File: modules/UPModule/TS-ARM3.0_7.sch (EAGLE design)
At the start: 83 parts, among them IC1 LPC1115, IC100 BD9G101, P1 , P10 , P11 , P12 , P13 , P14 , P2 , P3 , P4 , P5 , P6 , P7 , P8 , P9 , T1 BC856, T2 BCP52, T3 BC847, X1 EIB

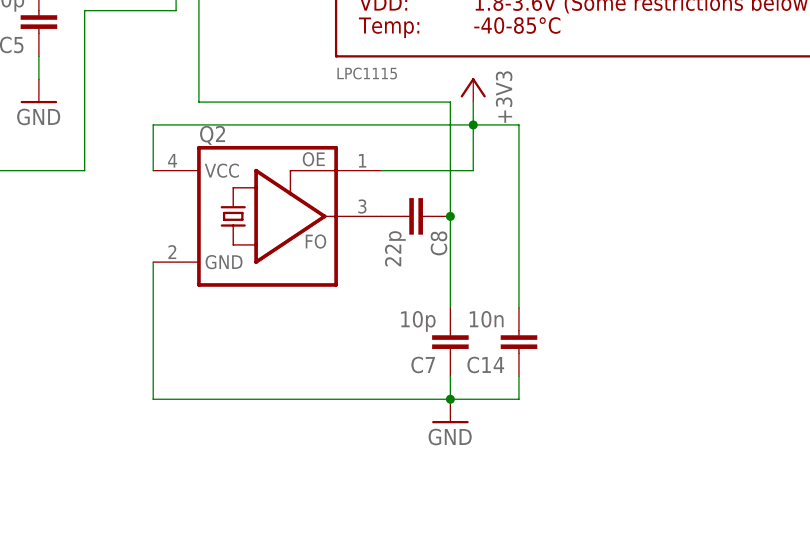
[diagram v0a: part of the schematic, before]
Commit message: value cap divider changed, micro vias with tstop, and hole free on top
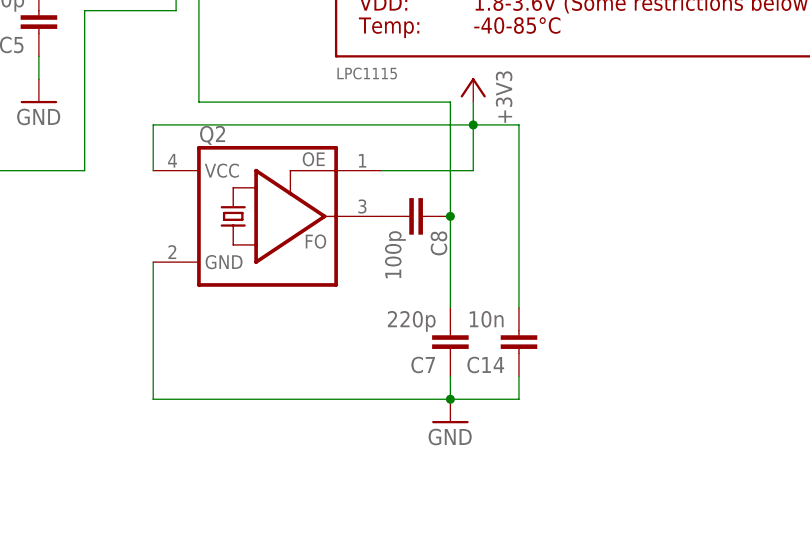
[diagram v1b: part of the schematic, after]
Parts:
- C7: value 10p -> 220p
- C8: value 22p -> 100p
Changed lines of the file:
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@@
 </part>
 <part name="Q2" library="crystal" deviceset="ASF*" device="" technology="L"/>
-<part name="C7" library="rcl" deviceset="C-EU" device="C1206" value="10p"/>
+<part name="C7" library="rcl" deviceset="C-EU" device="C1206" value="220p"/>
 <part name="P+11" library="supply1" deviceset="+3V3" device=""/>
 <part name="JP10" library="pinhead" deviceset="PINHD-1X1" device=""/>
-<part name="C8" library="rcl" deviceset="C-EU" device="C1206" value="22p"/>
+<part name="C8" library="rcl" deviceset="C-EU" device="C1206" value="100p"/>
 <part name="C14" library="rcl" deviceset="C-EU" device="C1206" value="10n"/>
 </parts>
